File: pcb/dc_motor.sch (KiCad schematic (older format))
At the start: 64 parts, among them J1 Conn_01x02, J2 Conn_01x04, J3 Conn_01x04, J4 Conn_01x07, Q1 Q_PMOS_GDS, Q2 BTN8982TA, Q3 BTN8982TA, U1 L7805, U2 INA226, U3 74AHC244

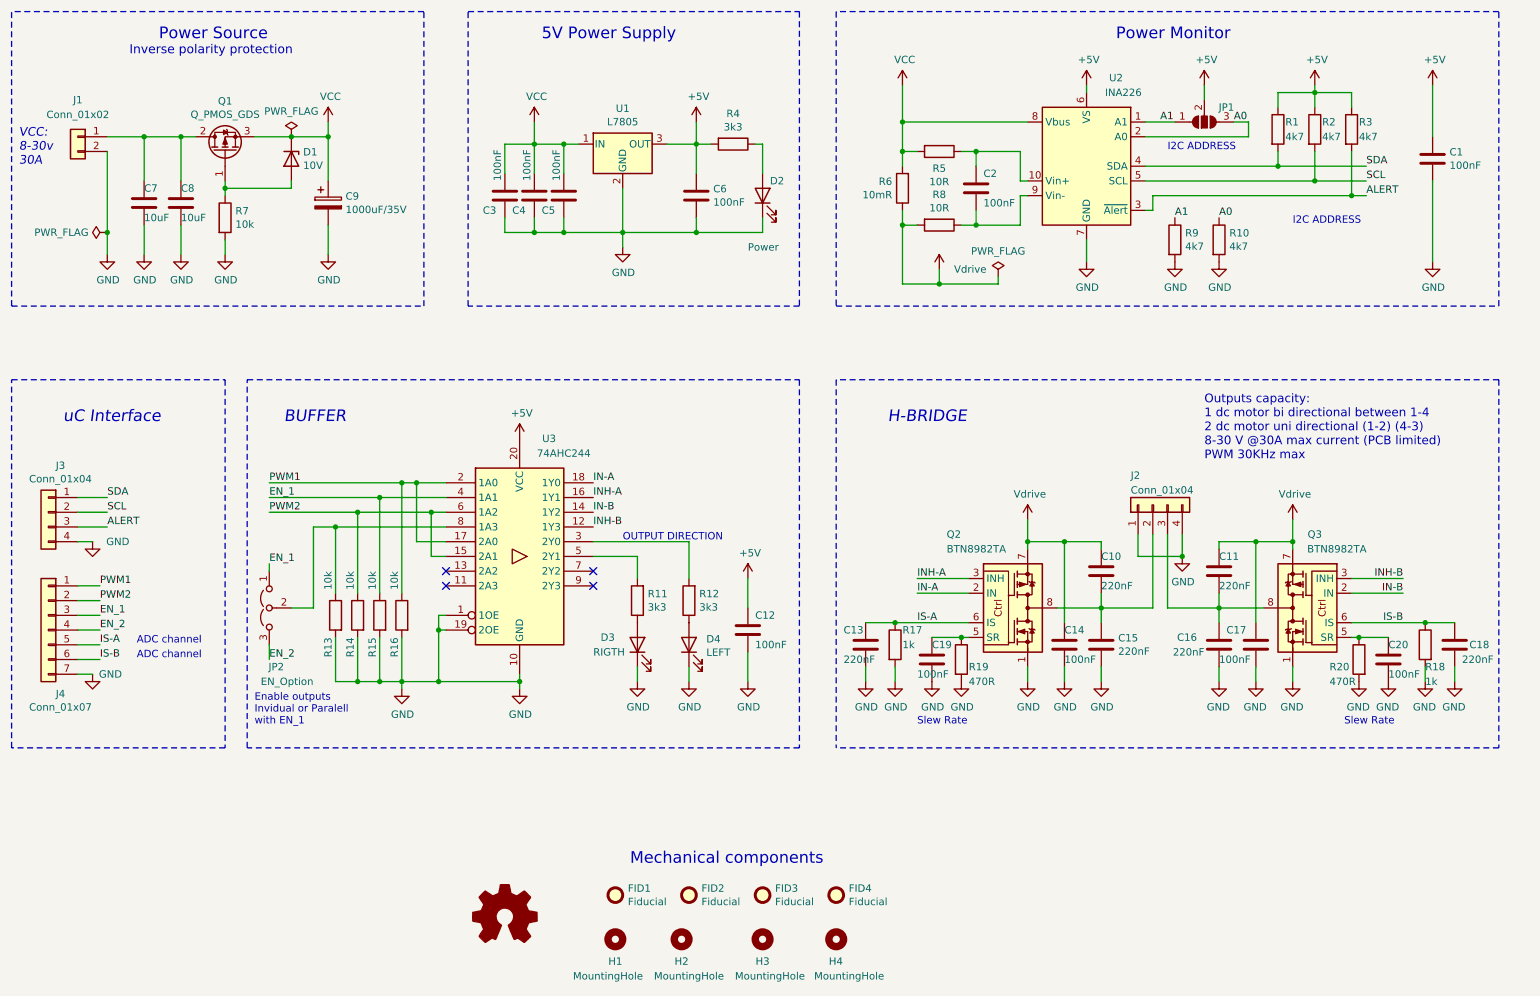
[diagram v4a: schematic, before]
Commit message: Rev1
Correcciones de primera revisión del profesor, hasta el esquemático.
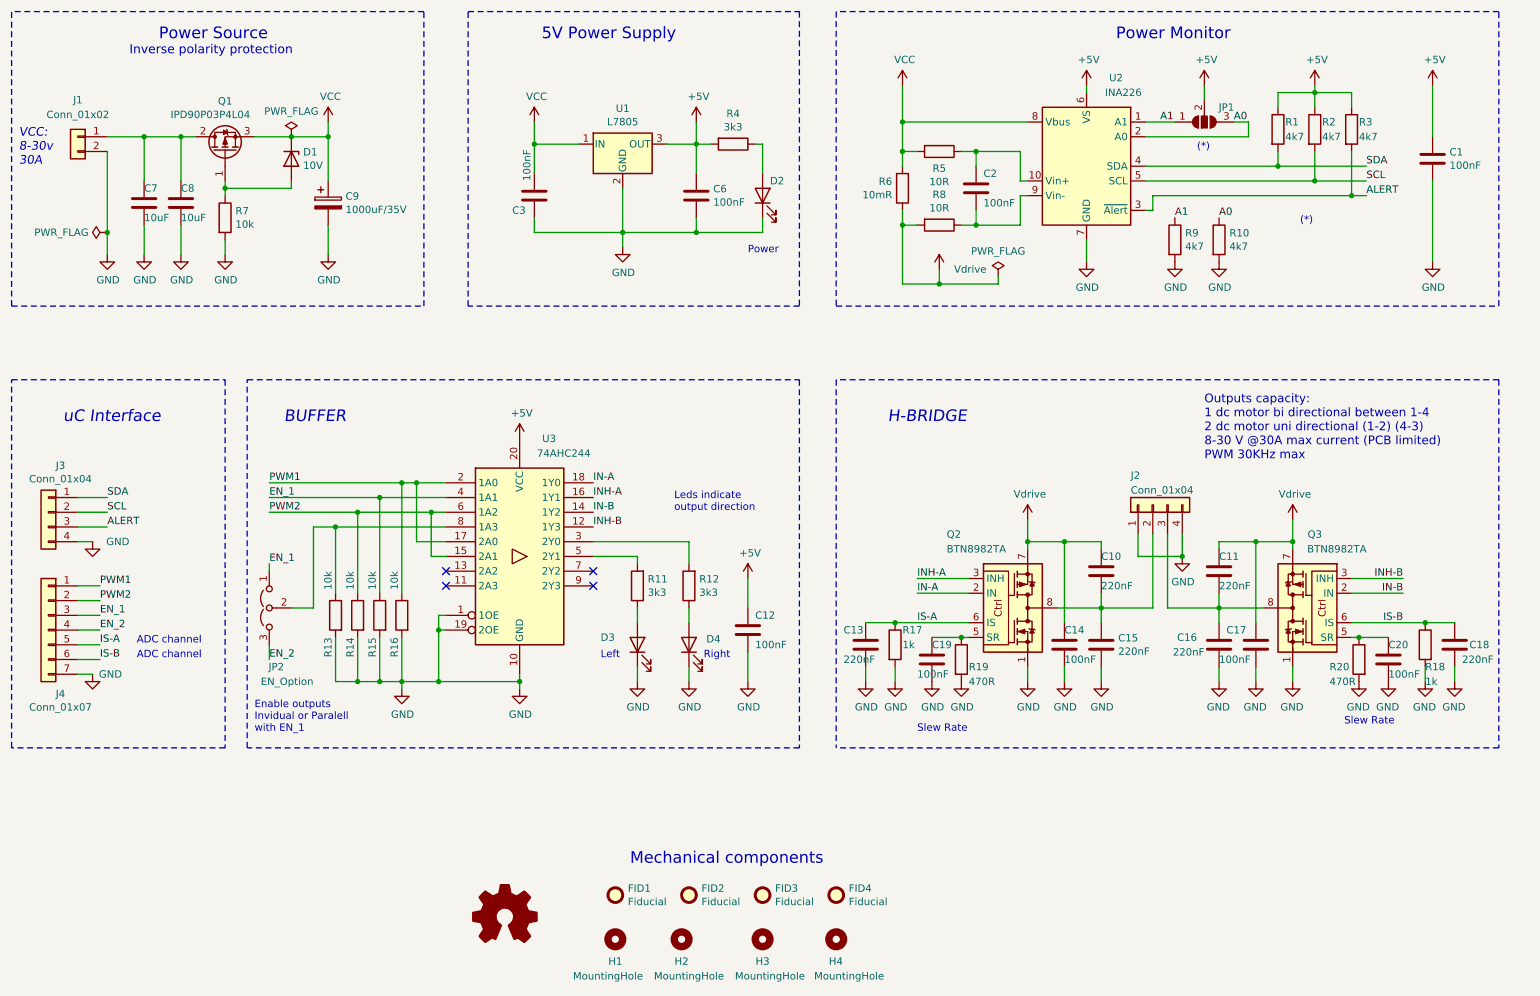
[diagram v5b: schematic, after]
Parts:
- removed C4, C5: 100nF, Capacitor_SMD:C_0603_1608Metric, symbol Device:C
- D2: value Power -> Green led 0603
- D3: value RIGTH -> Yellow led 0603
- D4: value LEFT -> Blue led 0603
- Q1: value Q_PMOS_GDS -> IPD90P03P4L04
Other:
- note added: "(*)"
- note added: "Leds indicate\noutput direction"
- note added: "Left"
- note added: "Power"
- note added: "Right"
- note removed: "I2C ADDRESS"
- note removed: "OUTPUT DIRECTION"
- moved on the sheet: C3, R11, R12
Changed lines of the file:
@@
 Text Label 9100 2400 0    50   ~ 0
 A0
-Text Notes 8750 1950 0    50   ~ 0
-I2C ADDRESS
+Text Notes 8950 1950 0    50   ~ 0
+(*)
 Wire Wire Line
 	9500 1650 9500 1550
@@
 P 5500 5300
 F 0 "D4" V 5539 5182 50  0000 R CNN
-F 1 "LEFT" V 5448 5182 50  0000 R CNN
+F 1 "Blue led 0603" V 5448 5182 50  0001 R CNN
 F 2 "LED_SMD:LED_0603_1608Metric" H 5500 5300 50  0001 C CNN
 F 3 "~" H 5500 5300 50  0001 C CNN
@@
 $EndComp
 Wire Wire Line
-	5050 2500 5050 2600
-Wire Wire Line
-	5050 2200 5050 2500
-Connection ~ 5050 2500
-Wire Wire Line
 	5550 2400 5550 2500
-Wire Wire Line
-	5550 2500 5050 2500
 $Comp
 L power:+5V #PWR08
@@
 P 6000 2250
 F 0 "D2" V 6100 2200 50  0000 R CNN
-F 1 "Power" V 5650 2350 50  0000 R CNN
+F 1 "Green led 0603" V 5650 2350 50  0001 R CNN
 F 2 "LED_SMD:LED_0603_1608Metric" H 6000 2250 50  0001 C CNN
 F 3 "~" H 6000 2250 50  0001 C CNN
@@
 Wire Wire Line
 	6950 1750 7800 1750
-$Comp
-L Device:R R12
-U 1 1 5F8FD498
-P 5500 5000
-F 0 "R12" H 5430 4954 50  0000 R CNN
-F 1 "3k3" H 5430 5045 50  0000 R CNN
-F 2 "Resistor_SMD:R_0603_1608Metric" V 5430 5000 50  0001 C CNN
-F 3 "~" H 5500 5000 50  0001 C CNN
-F 4 "RC0603JR-073K3L" H 5500 5000 50  0001 C CNN "Manufacturer Part Number"
-F 5 "311-3.3KGRCT-ND" H 5500 5000 50  0001 C CNN "Supplier 1 Part Number"
-	1    5500 5000
-	-1   0    0    1
-$EndComp
-Wire Wire Line
-	5500 4600 5500 4850
 Wire Wire Line
 	4850 4600 5500 4600
@@
 	1    0    0    -1
 $EndComp
-$Comp
-L Device:R R11
-U 1 1 5F8FD984
-P 5150 5000
-F 0 "R11" H 5080 4954 50  0000 R CNN
-F 1 "3k3" H 5080 5045 50  0000 R CNN
-F 2 "Resistor_SMD:R_0603_1608Metric" V 5080 5000 50  0001 C CNN
-F 3 "~" H 5150 5000 50  0001 C CNN
-F 4 "RC0603JR-073K3L" H 5150 5000 50  0001 C CNN "Manufacturer Part Number"
-F 5 "311-3.3KGRCT-ND" H 5150 5000 50  0001 C CNN "Supplier 1 Part Number"
-	1    5150 5000
-	-1   0    0    1
-$EndComp
-Wire Wire Line
-	5150 5450 5150 5550
-$Comp
-L Device:LED D3
-U 1 1 5F8FE631
-P 5150 5300
-F 0 "D3" V 5200 5550 50  0000 R CNN
-F 1 "RIGTH" V 5100 5600 50  0000 R CNN
-F 2 "LED_SMD:LED_0603_1608Metric" H 5150 5300 50  0001 C CNN
-F 3 "~" H 5150 5300 50  0001 C CNN
-F 4 "LTST-C191KSKT" H 5150 5300 50  0001 C CNN "Manufacturer Part Number"
-F 5 "160-1448-1-ND" H 5150 5300 50  0001 C CNN "Supplier 1 Part Number"
-	1    5150 5300
-	0    -1   -1   0
-$EndComp
-Text Notes 5050 4600 0    50   ~ 0
-OUTPUT DIRECTION
+Text Notes 5400 4400 0    50   ~ 0
+Leds indicate\noutput direction
 $Comp
 L Device:C C12
@@
 	1    0    0    -1
 $EndComp
-Text Notes 7050 5850 0    50   ~ 0
+Text Notes 7050 5900 0    50   ~ 0
 Slew Rate
 Text Notes 9950 5850 0    50   ~ 0
@@
 Text Label 2650 5400 0    50   ~ 0
 EN_2
-Text Notes 2550 5850 0    50   ~ 0
+Text Notes 2550 5900 0    50   ~ 0
 Enable outputs\nInvidual or Paralell\nwith EN_1
 Wire Wire Line
-	5150 4700 5150 4850
-Wire Wire Line
 	4850 4700 5150 4700
 $Bitmap
-Pos 9850 2700
+Pos 10000 2700
 Scale 1.000000
 Data
@@
 EndData
 $EndBitmap
-Text Notes 9600 2450 0    50   ~ 0
-I2C ADDRESS
+Text Notes 9650 2450 0    50   ~ 0
+(*)
 $Comp
 L power:Vdrive #PWR019
@@
 P 2350 1950
 F 0 "Q1" V 2692 1950 50  0000 C CNN
-F 1 "Q_PMOS_GDS" V 2601 1950 50  0000 C CNN
+F 1 "IPD90P03P4L04" V 2600 2050 50  0000 C CNN
 F 2 "Package_TO_SOT_SMD:TO-252-2" H 2550 2050 50  0001 C CNN
 F 3 "https://www.infineon.com/dgdl/Infineon-IPD90P03P4L_04-DS-v01_00-en.pdf?folderId=db3a304314dca3890114ef902baa05f9&fileId=db3a30431ddc9372011e07e8373a27c4&ack=t" H 2350 1950 50  0001 C CNN
@@
 Wire Wire Line
 	2650 5300 2650 5400
-$Comp
-L Device:C C5
-U 1 1 5FA39240
-P 4650 2250
-F 0 "C5" H 4500 2150 50  0000 L CNN
-F 1 "100nF" V 4600 2350 50  0000 L CNN
-F 2 "Capacitor_SMD:C_0603_1608Metric" H 4688 2100 50  0001 C CNN
-F 3 "~" H 4650 2250 50  0001 C CNN
-F 4 "GMK107B7104KAHT" H 4650 2250 50  0001 C CNN "Manufacturer Part Number"
-F 5 "587-3354-1-ND" H 4650 2250 50  0001 C CNN "Supplier 1 Part Number"
-	1    4650 2250
-	1    0    0    -1
-$EndComp
-Wire Wire Line
-	4250 2500 4250 2400
-Wire Wire Line
-	4250 2500 4450 2500
-Wire Wire Line
-	4450 2400 4450 2500
-Connection ~ 4450 2500
-Wire Wire Line
-	4450 2500 4650 2500
-Wire Wire Line
-	4650 2400 4650 2500
-Connection ~ 4650 2500
-Wire Wire Line
-	4650 2500 5050 2500
-Wire Wire Line
-	4250 2100 4250 1900
-Wire Wire Line
-	4650 2100 4650 1900
 Wire Wire Line
-	4650 1900 4750 1900
-Connection ~ 4650 1900
-Connection ~ 4450 1900
-Wire Wire Line
-	4450 1900 4650 1900
+	4450 2500 4450 2400
 Wire Wire Line
 	4450 2100 4450 1900
-Wire Wire Line
-	4250 1900 4450 1900
+Connection ~ 4450 1900
 $Comp
 L power:VCC #PWR07
@@
 	4450 1750 4450 1900
 $Comp
-L Device:C C4
-U 1 1 5FA2F27C
+L Device:C C3
+U 1 1 5FA252F9
 P 4450 2250
-F 0 "C4" H 4300 2150 50  0000 L CNN
+F 0 "C3" H 4300 2150 50  0000 L CNN
 F 1 "100nF" V 4400 2350 50  0000 L CNN
 F 2 "Capacitor_SMD:C_0603_1608Metric" H 4488 2100 50  0001 C CNN
@@
 	1    0    0    -1
 $EndComp
+Wire Wire Line
+	5150 5450 5150 5550
+Wire Wire Line
+	5150 4700 5150 4750
 $Comp
-L Device:C C3
-U 1 1 5FA252F9
-P 4250 2250
-F 0 "C3" H 4100 2150 50  0000 L CNN
-F 1 "100nF" V 4200 2350 50  0000 L CNN
-F 2 "Capacitor_SMD:C_0603_1608Metric" H 4288 2100 50  0001 C CNN
-F 3 "~" H 4250 2250 50  0001 C CNN
-F 4 "GMK107B7104KAHT" H 4250 2250 50  0001 C CNN "Manufacturer Part Number"
-F 5 "587-3354-1-ND" H 4250 2250 50  0001 C CNN "Supplier 1 Part Number"
-	1    4250 2250
-	1    0    0    -1
+L Device:R R11
+U 1 1 5F8FD984
+P 5150 4900
+F 0 "R11" H 5080 4854 50  0000 R CNN
+F 1 "3k3" H 5080 4945 50  0000 R CNN
+F 2 "Resistor_SMD:R_0603_1608Metric" V 5080 4900 50  0001 C CNN
+F 3 "~" H 5150 4900 50  0001 C CNN
+F 4 "RC0603JR-073K3L" H 5150 4900 50  0001 C CNN "Manufacturer Part Number"
+F 5 "311-3.3KGRCT-ND" H 5150 4900 50  0001 C CNN "Supplier 1 Part Number"
+	1    5150 4900
+	-1   0    0    1
+$EndComp
+Wire Wire Line
+	5150 5150 5150 5050
+Wire Wire Line
+	5500 4600 5500 4750
+$Comp
+L Device:R R12
+U 1 1 5F8FD498
+P 5500 4900
+F 0 "R12" H 5430 4854 50  0000 R CNN
+F 1 "3k3" H 5430 4945 50  0000 R CNN
+F 2 "Resistor_SMD:R_0603_1608Metric" V 5430 4900 50  0001 C CNN
+F 3 "~" H 5500 4900 50  0001 C CNN
+F 4 "RC0603JR-073K3L" H 5500 4900 50  0001 C CNN "Manufacturer Part Number"
+F 5 "311-3.3KGRCT-ND" H 5500 4900 50  0001 C CNN "Supplier 1 Part Number"
+	1    5500 4900
+	-1   0    0    1
 $EndComp
+Wire Wire Line
+	5500 5150 5500 5050
+$Comp
+L Device:LED D3
+U 1 1 5F8FE631
+P 5150 5300
+F 0 "D3" V 5200 5550 50  0000 R CNN
+F 1 "Yellow led 0603" V 5100 5600 50  0001 R CNN
+F 2 "LED_SMD:LED_0603_1608Metric" H 5150 5300 50  0001 C CNN
+F 3 "~" H 5150 5300 50  0001 C CNN
+F 4 "LTST-C191KSKT" H 5150 5300 50  0001 C CNN "Manufacturer Part Number"
+F 5 "160-1448-1-ND" H 5150 5300 50  0001 C CNN "Supplier 1 Part Number"
+	1    5150 5300
+	0    -1   -1   0
+$EndComp
+Text Notes 5900 2650 0    50   ~ 0
+Power
+Text Notes 4900 5400 0    50   ~ 0
+Left
+Text Notes 5600 5400 0    50   ~ 0
+Right
+Wire Wire Line
+	4450 1900 4750 1900
+Wire Wire Line
+	4450 2500 5050 2500
+Wire Wire Line
+	5050 2200 5050 2500
+Connection ~ 5050 2500
+Wire Wire Line
+	5050 2500 5550 2500
+Wire Wire Line
+	5050 2500 5050 2600
 $EndSCHEMATC

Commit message: Placement
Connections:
- net ALERT: now also J3.2 (Pin_2); no longer J3.3 (Pin_3)
- net EN_1: now also J4.2 (Pin_2); no longer J4.3 (Pin_3)
- net GND: now also J3.1 (Pin_1); no longer J3.4 (Pin_4)
- net PWM2: now also J4.3 (Pin_3); no longer J4.2 (Pin_2)
- net SCL: now also J3.4 (Pin_4); no longer J3.2 (Pin_2)
- net SDA: now also J3.3 (Pin_3); no longer J3.1 (Pin_1)
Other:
- moved on the sheet: J3
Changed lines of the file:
@@
 Text Notes 1750 5400 0    50   ~ 0
 ADC channel
-Wire Wire Line
-	1350 4300 1550 4300
-Wire Wire Line
-	1350 4400 1550 4400
-Wire Wire Line
-	1350 4500 1550 4500
 $Comp
 L Connector_Generic:Conn_01x04 J3
 U 1 1 5FB3C4A6
 P 1150 4400
-F 0 "J3" H 1068 4717 50  0000 C CNN
-F 1 "Conn_01x04" H 1068 4626 50  0000 C CNN
+F 0 "J3" H 1068 3975 50  0000 C CNN
+F 1 "Conn_01x04" H 1068 4066 50  0000 C CNN
 F 2 "Connector_Molex:Molex_KK-254_AE-6410-04A_1x04_P2.54mm_Vertical" H 1150 4400 50  0001 C CNN
 F 3 "https://www.molex.com/pdm_docs/ps/PS-10-07-001.pdf" H 1150 4400 50  0001 C CNN
@@
 F 5 "WM4202-ND" H 1150 4400 50  0001 C CNN "Supplier 1 Part Number"
 	1    1150 4400
-	-1   0    0    -1
+	-1   0    0    1
 $EndComp
 Wire Wire Line
@@
 IS-A
 $Comp
-L power:GND #PWR023
-U 1 1 5FA79917
-P 1450 4600
-F 0 "#PWR023" H 1450 4350 50  0001 C CNN
-F 1 "GND" H 1700 4600 50  0000 R CNN
-F 2 "" H 1450 4600 50  0001 C CNN
-F 3 "" H 1450 4600 50  0001 C CNN
-	1    1450 4600
-	1    0    0    -1
-$EndComp
-$Comp
 L power:GND #PWR026
 U 1 1 5FA788B6
@@
 	1    0    0    -1
 $EndComp
-Text Label 1550 4500 0    50   ~ 0
-ALERT
-Text Label 1550 4400 0    50   ~ 0
-SCL
-Text Label 1550 4300 0    50   ~ 0
-SDA
 Text Label 1500 5200 0    50   ~ 0
 EN_2
-Text Label 1500 5100 0    50   ~ 0
-EN_1
 Text Label 1500 5000 0    50   ~ 0
+EN_1
+Text Label 1500 5100 0    50   ~ 0
 PWM2
 Text Label 1500 4900 0    50   ~ 0
@@
 	6950 2450 6950 2850
 $Comp
-L power:Vdrive #PWR021
-U 1 1 5F6F43EA
-P 7800 4450
-F 0 "#PWR021" H 7600 4300 50  0001 C CNN
-F 1 "Vdrive" H 7815 4623 50  0000 C CNN
-F 2 "" H 7800 4450 50  0001 C CNN
-F 3 "" H 7800 4450 50  0001 C CNN
-	1    7800 4450
-	1    0    0    -1
-$EndComp
-$Comp
 L power:Vdrive #PWR022
 U 1 1 5F707987
@@
 	8050 4600 7800 4600
 Connection ~ 8050 4600
-Connection ~ 7800 4600
-Wire Wire Line
-	7800 4600 7800 4450
 $Comp
 L power:PWR_FLAG #FLG02
@@
 	1350 5500 1450 5500
 Wire Wire Line
-	1450 4600 1350 4600
-Wire Wire Line
 	7200 2750 7200 2850
 Wire Wire Line
@@
 Wire Wire Line
 	5050 2500 5050 2600
+Connection ~ 7800 4600
+Wire Wire Line
+	7800 4600 7800 4450
+$Comp
+L power:Vdrive #PWR021
+U 1 1 5F6F43EA
+P 7800 4450
+F 0 "#PWR021" H 7600 4300 50  0001 C CNN
+F 1 "Vdrive" H 7815 4623 50  0000 C CNN
+F 2 "" H 7800 4450 50  0001 C CNN
+F 3 "" H 7800 4450 50  0001 C CNN
+	1    7800 4450
+	1    0    0    -1
+$EndComp
+Text Label 1350 4200 0    50   ~ 0
+SCL
+Text Label 1350 4300 0    50   ~ 0
+SDA
+Text Label 1350 4400 0    50   ~ 0
+ALERT
+$Comp
+L power:GND #PWR023
+U 1 1 5FA79917
+P 1400 4600
+F 0 "#PWR023" H 1400 4350 50  0001 C CNN
+F 1 "GND" H 1650 4600 50  0000 R CNN
+F 2 "" H 1400 4600 50  0001 C CNN
+F 3 "" H 1400 4600 50  0001 C CNN
+	1    1400 4600
+	1    0    0    -1
+$EndComp
+Wire Wire Line
+	1400 4600 1400 4500
+Wire Wire Line
+	1400 4500 1350 4500
 $EndSCHEMATC

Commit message: board dimension
change 1 capacitor value.
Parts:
- C13, C18: value 220nF -> 1nF; Manufacturer Part Number GCJ188R71H224KA01D -> GCM188R91H102KA37D; Supplier 1 Part Number 490-14410-1-ND -> 490-14360-1-ND
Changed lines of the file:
@@
 P 10700 5300
 F 0 "C18" H 10600 5300 50  0000 R CNN
-F 1 "220nF" H 10650 5200 50  0000 R CNN
+F 1 "1nF" H 10650 5200 50  0000 R CNN
 F 2 "Capacitor_SMD:C_0603_1608Metric" H 10738 5150 50  0001 C CNN
 F 3 "~" H 10700 5300 50  0001 C CNN
-F 4 "GCJ188R71H224KA01D" H 10700 5300 50  0001 C CNN "Manufacturer Part Number"
-F 5 "490-14410-1-ND" H 10700 5300 50  0001 C CNN "Supplier 1 Part Number"
+F 4 "GCM188R91H102KA37D" H 10700 5300 50  0001 C CNN "Manufacturer Part Number"
+F 5 "490-14360-1-ND" H 10700 5300 50  0001 C CNN "Supplier 1 Part Number"
 	1    10700 5300
 	-1   0    0    -1
@@
 P 6700 5300
 F 0 "C13" H 6550 5400 50  0000 L CNN
-F 1 "220nF" H 6550 5200 50  0000 L CNN
+F 1 "1nF" H 6550 5200 50  0000 L CNN
 F 2 "Capacitor_SMD:C_0603_1608Metric" H 6738 5150 50  0001 C CNN
 F 3 "~" H 6700 5300 50  0001 C CNN
-F 4 "GCJ188R71H224KA01D" H 6700 5300 50  0001 C CNN "Manufacturer Part Number"
-F 5 "490-14410-1-ND" H 6700 5300 50  0001 C CNN "Supplier 1 Part Number"
+F 4 "GCM188R91H102KA37D" H 6700 5300 50  0001 C CNN "Manufacturer Part Number"
+F 5 "490-14360-1-ND" H 6700 5300 50  0001 C CNN "Supplier 1 Part Number"
 	1    6700 5300
 	1    0    0    -1
@@
 	7350 5250 7400 5250
 $Comp
-L Device:R R19
-U 1 1 5F5FB08E
-P 7350 5400
-F 0 "R19" H 7400 5350 50  0000 L CNN
-F 1 "470R" H 7400 5250 50  0000 L CNN
-F 2 "Resistor_SMD:R_0603_1608Metric" V 7280 5400 50  0001 C CNN
-F 3 "~" H 7350 5400 50  0001 C CNN
-F 4 "RC0603FR-07470RL" H 7350 5400 50  0001 C CNN "Manufacturer Part Number"
-F 5 "311-470HRCT-ND" H 7350 5400 50  0001 C CNN "Supplier 1 Part Number"
-	1    7350 5400
-	1    0    0    -1
-$EndComp
-$Comp
 L Device:R R17
 U 1 1 5F5FB088
@@
 Wire Wire Line
 	1400 4500 1350 4500
+$Comp
+L Device:R R19
+U 1 1 5F5FB08E
+P 7350 5400
+F 0 "R19" H 7400 5350 50  0000 L CNN
+F 1 "470R" H 7400 5250 50  0000 L CNN
+F 2 "Resistor_SMD:R_0603_1608Metric" V 7280 5400 50  0001 C CNN
+F 3 "~" H 7350 5400 50  0001 C CNN
+F 4 "RC0603FR-07470RL" H 7350 5400 50  0001 C CNN "Manufacturer Part Number"
+F 5 "311-470HRCT-ND" H 7350 5400 50  0001 C CNN "Supplier 1 Part Number"
+	1    7350 5400
+	1    0    0    -1
+$EndComp
 $EndSCHEMATC
